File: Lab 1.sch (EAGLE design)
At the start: 8 parts

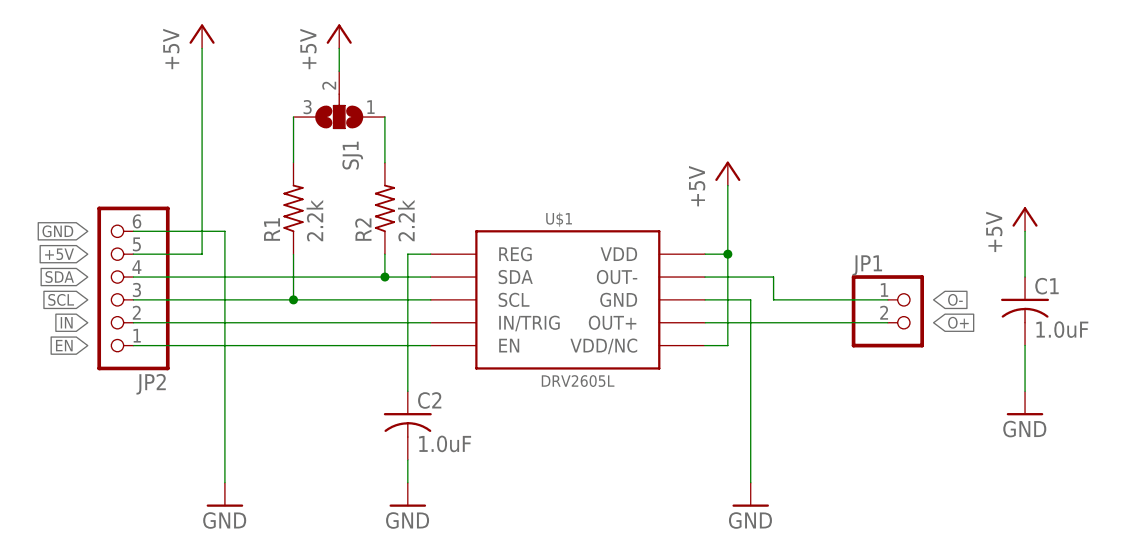
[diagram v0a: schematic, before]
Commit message: Added Ground Plane. Added Filter Capacitor
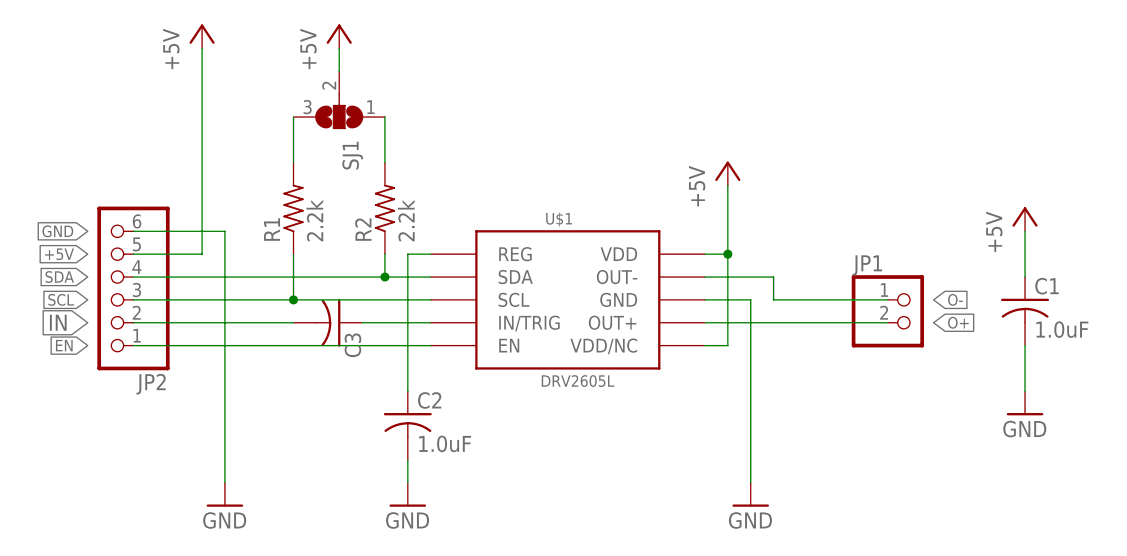
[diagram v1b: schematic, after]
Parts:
- added C3: (no value), rcl:C-USC0805
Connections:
- new net N$2: C3.1, U$1.IN/TRIG
- net IN: now also C3.2; no longer U$1.IN/TRIG
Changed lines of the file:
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@@
 <?xml version="1.0" encoding="utf-8"?>
 <!DOCTYPE eagle SYSTEM "eagle.dtd">
-<eagle version="9.1.1">
+<eagle version="9.5.0">
 <drawing>
 <settings>
@@
 <layers>
 <layer number="1" name="Top" color="4" fill="1" visible="no" active="no"/>
+<layer number="2" name="Route2" color="1" fill="3" visible="no" active="no"/>
+<layer number="3" name="Route3" color="4" fill="3" visible="no" active="no"/>
+<layer number="4" name="Route4" color="1" fill="4" visible="no" active="no"/>
+<layer number="5" name="Route5" color="4" fill="4" visible="no" active="no"/>
+<layer number="6" name="Route6" color="1" fill="8" visible="no" active="no"/>
+<layer number="7" name="Route7" color="4" fill="8" visible="no" active="no"/>
+<layer number="8" name="Route8" color="1" fill="2" visible="no" active="no"/>
+<layer number="9" name="Route9" color="4" fill="2" visible="no" active="no"/>
+<layer number="10" name="Route10" color="1" fill="7" visible="no" active="no"/>
+<layer number="11" name="Route11" color="4" fill="7" visible="no" active="no"/>
+<layer number="12" name="Route12" color="1" fill="5" visible="no" active="no"/>
+<layer number="13" name="Route13" color="4" fill="5" visible="no" active="no"/>
+<layer number="14" name="Route14" color="1" fill="6" visible="no" active="no"/>
+<layer number="15" name="Route15" color="4" fill="6" visible="no" active="no"/>
 <layer number="16" name="Bottom" color="1" fill="1" visible="no" active="no"/>
 <layer number="17" name="Pads" color="2" fill="1" visible="no" active="no"/>
@@
 <part name="GND3" library="supply1" library_urn="urn:adsk.eagle:library:371" deviceset="GND" device=""/>
 <part name="GND4" library="supply1" library_urn="urn:adsk.eagle:library:371" deviceset="GND" device=""/>
+<part name="C3" library="rcl" library_urn="urn:adsk.eagle:library:334" deviceset="C-US" device="C0805" package3d_urn="urn:adsk.eagle:package:23617/2"/>
 </parts>
 <sheets>
@@
 </plain>
 <instances>
-<instance part="U$1" gate="DRV2605" x="68.58" y="76.2"/>
-<instance part="P+1" gate="1" x="86.36" y="91.44"/>
-<instance part="GND1" gate="1" x="88.9" y="53.34"/>
-<instance part="C1" gate="G$1" x="119.38" y="76.2"/>
-<instance part="R1" gate="G$1" x="38.1" y="86.36" rot="R90"/>
-<instance part="JP1" gate="G$1" x="106.68" y="73.66"/>
-<instance part="JP2" gate="A" x="17.78" y="78.74" rot="R180"/>
-<instance part="GND2" gate="1" x="30.48" y="53.34"/>
-<instance part="P+2" gate="1" x="27.94" y="106.68"/>
-<instance part="C2" gate="G$1" x="50.8" y="63.5"/>
-<instance part="R2" gate="G$1" x="48.26" y="86.36" rot="R90"/>
-<instance part="P+3" gate="1" x="43.18" y="106.68"/>
-<instance part="SJ1" gate="G$1" x="43.18" y="96.52" rot="R270"/>
-<instance part="P+4" gate="1" x="119.38" y="86.36"/>
-<instance part="GND3" gate="1" x="119.38" y="63.5"/>
-<instance part="GND4" gate="1" x="50.8" y="53.34"/>
+<instance part="U$1" gate="DRV2605" x="68.58" y="76.2" smashed="yes">
+<attribute name="NAME" x="66.04" y="84.582" size="1.27" layer="95"/>
+<attribute name="VALUE" x="65.532" y="66.548" size="1.27" layer="96"/>
+</instance>
+<instance part="P+1" gate="1" x="86.36" y="91.44" smashed="yes">
+<attribute name="VALUE" x="83.82" y="86.36" size="1.778" layer="96" rot="R90"/>
+</instance>
+<instance part="GND1" gate="1" x="88.9" y="53.34" smashed="yes">
+<attribute name="VALUE" x="86.36" y="50.8" size="1.778" layer="96"/>
+</instance>
+<instance part="C1" gate="G$1" x="119.38" y="76.2" smashed="yes">
+<attribute name="NAME" x="120.396" y="76.835" size="1.778" layer="95"/>
+<attribute name="VALUE" x="120.396" y="72.009" size="1.778" layer="96"/>
+</instance>
+<instance part="R1" gate="G$1" x="38.1" y="86.36" smashed="yes" rot="R90">
+<attribute name="NAME" x="36.6014" y="82.55" size="1.778" layer="95" rot="R90"/>
+<attribute name="VALUE" x="41.402" y="82.55" size="1.778" layer="96" rot="R90"/>
+</instance>
+<instance part="JP1" gate="G$1" x="106.68" y="73.66" smashed="yes">
+<attribute name="NAME" x="100.33" y="79.375" size="1.778" layer="95"/>
+<attribute name="VALUE" x="100.33" y="68.58" size="1.778" layer="96"/>
+</instance>
+<instance part="JP2" gate="A" x="17.78" y="78.74" smashed="yes" rot="R180">
+<attribute name="NAME" x="24.13" y="67.945" size="1.778" layer="95" rot="R180"/>
+<attribute name="VALUE" x="24.13" y="88.9" size="1.778" layer="96" rot="R180"/>
+</instance>
+<instance part="GND2" gate="1" x="30.48" y="53.34" smashed="yes">
+<attribute name="VALUE" x="27.94" y="50.8" size="1.778" layer="96"/>
+</instance>
+<instance part="P+2" gate="1" x="27.94" y="106.68" smashed="yes">
+<attribute name="VALUE" x="25.4" y="101.6" size="1.778" layer="96" rot="R90"/>
+</instance>
+<instance part="C2" gate="G$1" x="50.8" y="63.5" smashed="yes">
+<attribute name="NAME" x="51.816" y="64.135" size="1.778" layer="95"/>
+<attribute name="VALUE" x="51.816" y="59.309" size="1.778" layer="96"/>
+</instance>
+<instance part="R2" gate="G$1" x="48.26" y="86.36" smashed="yes" rot="R90">
+<attribute name="NAME" x="46.7614" y="82.55" size="1.778" layer="95" rot="R90"/>
+<attribute name="VALUE" x="51.562" y="82.55" size="1.778" layer="96" rot="R90"/>
+</instance>
+<instance part="P+3" gate="1" x="43.18" y="106.68" smashed="yes">
+<attribute name="VALUE" x="40.64" y="101.6" size="1.778" layer="96" rot="R90"/>
+</instance>
+<instance part="SJ1" gate="G$1" x="43.18" y="96.52" smashed="yes" rot="R270">
+<attribute name="NAME" x="43.561" y="93.98" size="1.778" layer="95" rot="R270"/>
+<attribute name="VALUE" x="41.275" y="93.98" size="1.778" layer="96" rot="R270"/>
+</instance>
+<instance part="P+4" gate="1" x="119.38" y="86.36" smashed="yes">
+<attribute name="VALUE" x="116.84" y="81.28" size="1.778" layer="96" rot="R90"/>
+</instance>
+<instance part="GND3" gate="1" x="119.38" y="63.5" smashed="yes">
+<attribute name="VALUE" x="116.84" y="60.96" size="1.778" layer="96"/>
+</instance>
+<instance part="GND4" gate="1" x="50.8" y="53.34" smashed="yes">
+<attribute name="VALUE" x="48.26" y="50.8" size="1.778" layer="96"/>
+</instance>
+<instance part="C3" gate="G$1" x="43.18" y="73.66" smashed="yes" rot="R270">
+<attribute name="NAME" x="43.815" y="72.644" size="1.778" layer="95" rot="R270"/>
+<attribute name="VALUE" x="38.989" y="72.644" size="1.778" layer="96" rot="R270"/>
+</instance>
 </instances>
 <busses>
@@
 </segment>
 </net>
-<net name="IN" class="0">
-<segment>
-<pinref part="U$1" gate="DRV2605" pin="IN/TRIG"/>
-<pinref part="JP2" gate="A" pin="2"/>
-<wire x1="53.34" y1="73.66" x2="20.32" y2="73.66" width="0.1524" layer="91"/>
-<label x="15.24" y="73.66" size="1.27" layer="95" rot="R180" xref="yes"/>
-</segment>
-</net>
 <net name="EN" class="0">
 <segment>
@@
 </segment>
 </net>
+<net name="IN" class="0">
+<segment>
+<pinref part="JP2" gate="A" pin="2"/>
+<pinref part="C3" gate="G$1" pin="2"/>
+<wire x1="20.32" y1="73.66" x2="38.1" y2="73.66" width="0.1524" layer="91"/>
+<label x="15.24" y="73.66" size="1.778" layer="95" rot="R180" xref="yes"/>
+</segment>
+</net>
+<net name="N$2" class="0">
+<segment>
+<pinref part="C3" gate="G$1" pin="1"/>
+<pinref part="U$1" gate="DRV2605" pin="IN/TRIG"/>
+<wire x1="45.72" y1="73.66" x2="53.34" y2="73.66" width="0.1524" layer="91"/>
+</segment>
+</net>
